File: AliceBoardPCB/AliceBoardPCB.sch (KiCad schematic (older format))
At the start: 1 part

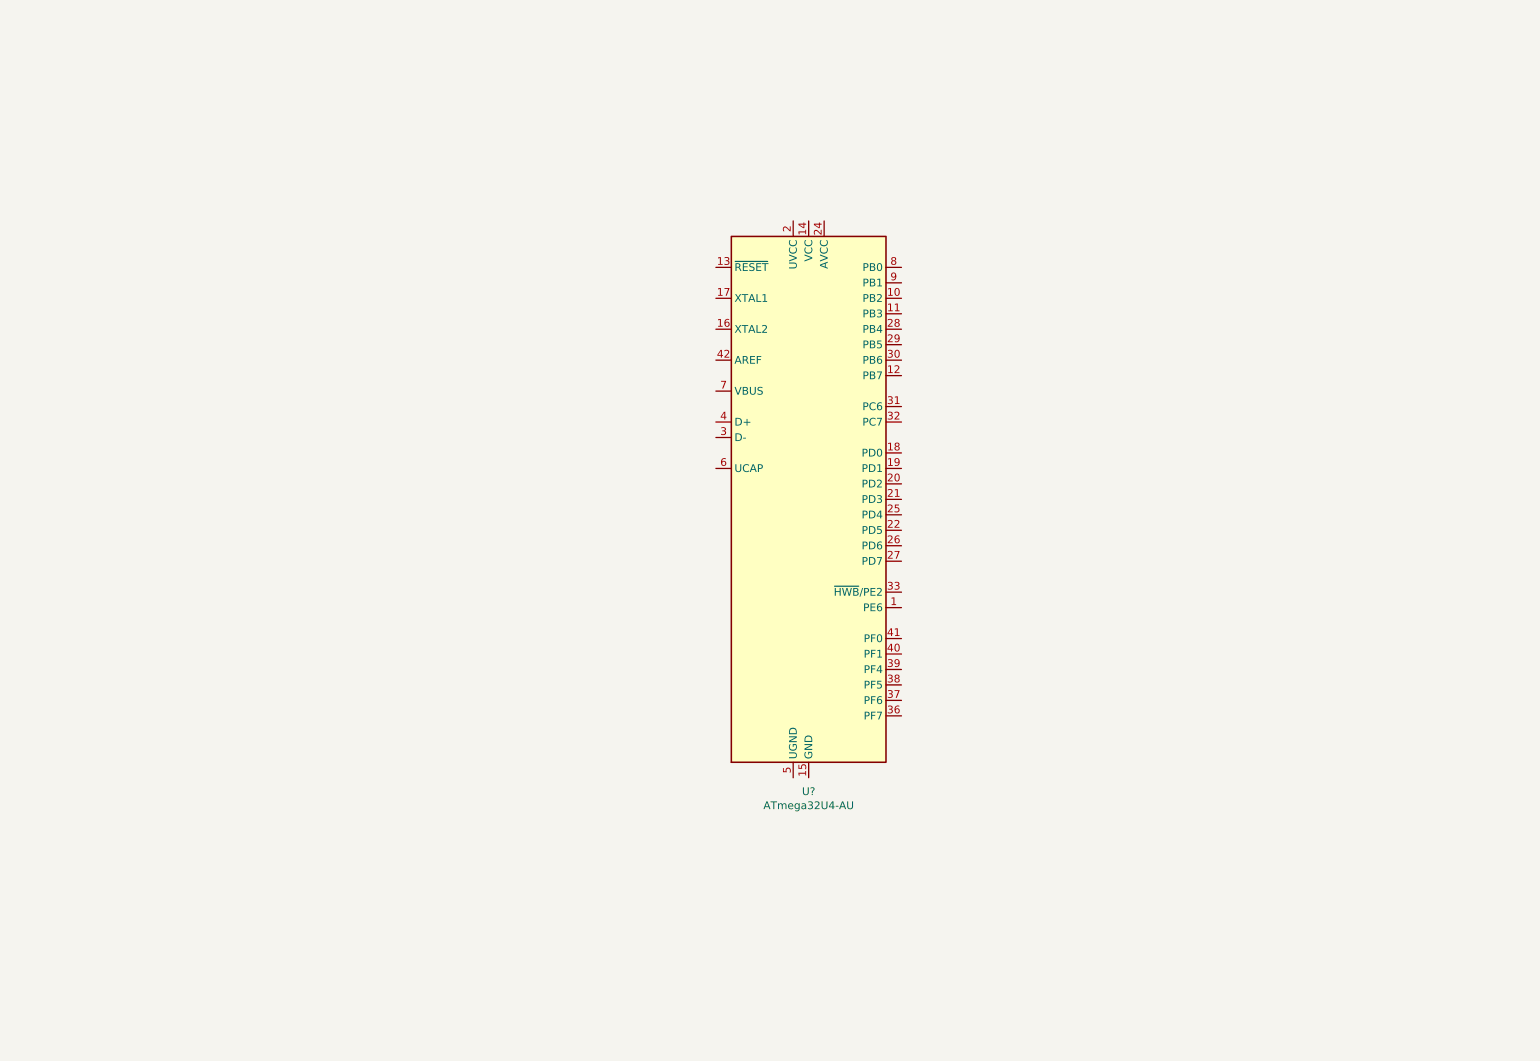
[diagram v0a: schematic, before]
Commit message: Schematic and Acrylic Case
Finished the pcb schematic and im starting the acrylic case.
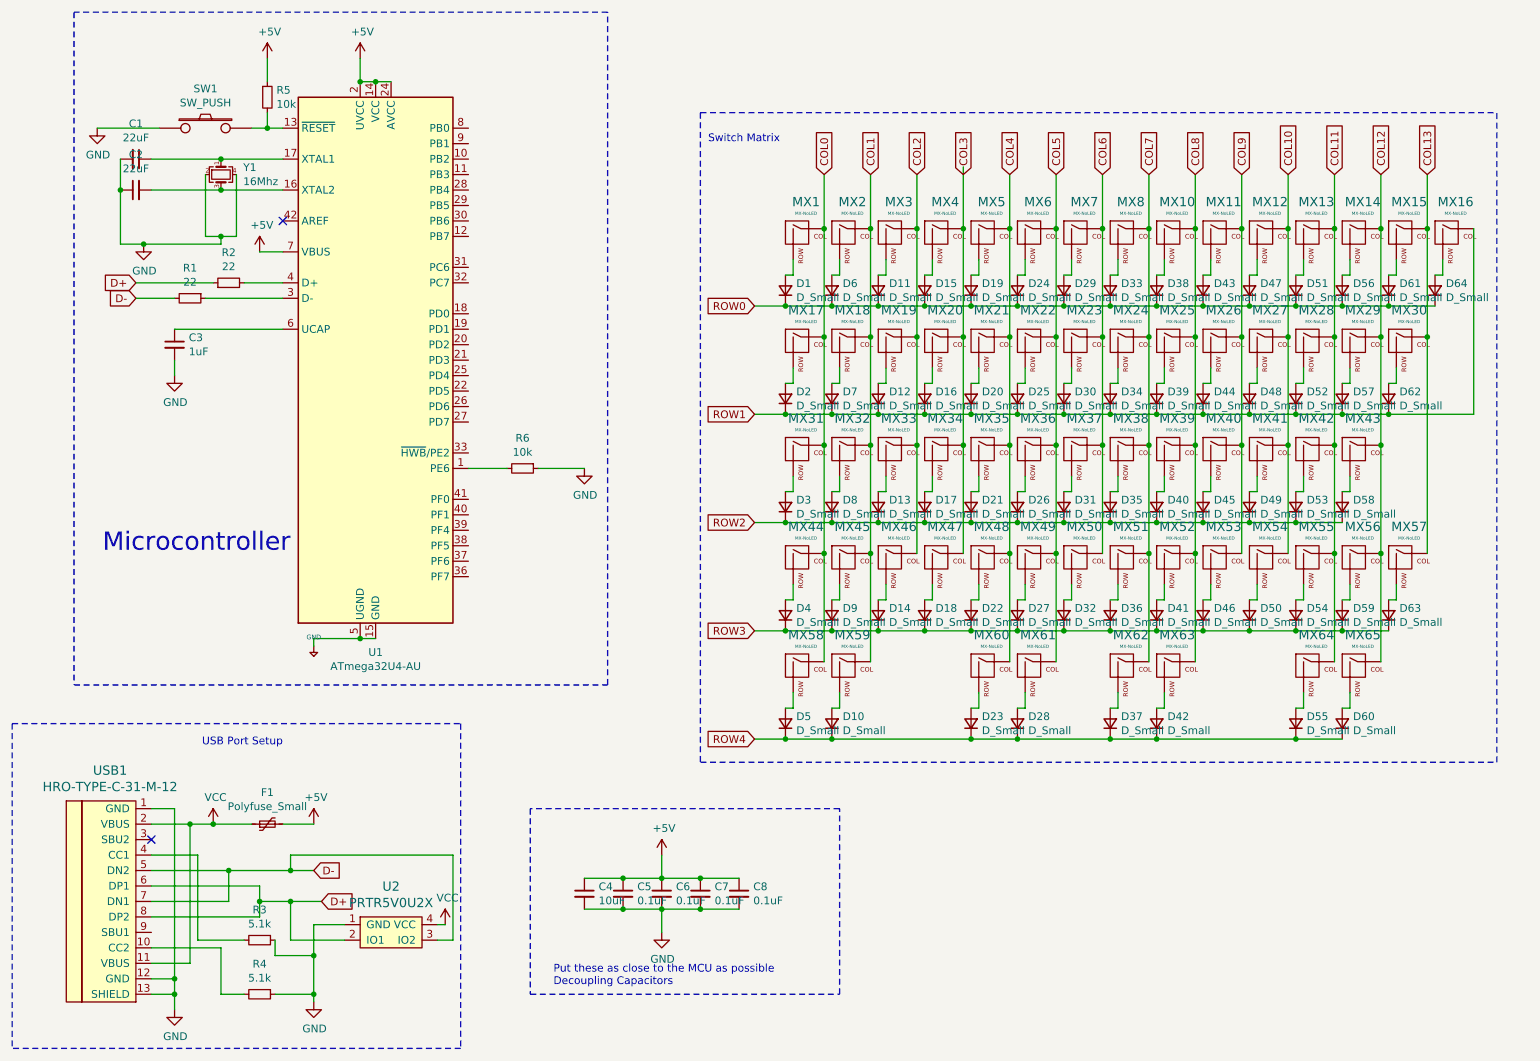
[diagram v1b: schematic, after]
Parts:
- added C1, C2: 22uF, Capacitor_SMD:C_0805_2012Metric, symbol Device:C_Small
- added C3: 1uF, Capacitor_SMD:C_0805_2012Metric, symbol Device:C_Small
- added C4: 10uF, Capacitor_SMD:C_0805_2012Metric, symbol Device:C_Small
- added C5, C6, C7, C8: 0.1uF, Capacitor_SMD:C_0805_2012Metric, symbol Device:C_Small
- added D1, D10, D11, D12, D13, D14, D15, D16, D17, D18, D19, D2, D20, D21, D22, D23, D24, D25, D26, D27, D28, D29, D3, D30, D31, D32, D33, D34, D35, D36, D37, D38, D39, D4, D40, D41, D42, D43, D44, D45, D46, D47, D48, D49, D5, D50, D51, D52, D53, D54, D55, D56, D57, D58, D59, D6, D60, D61, D62, D63, D64, D7, D8, D9: D_Small, Diode_SMD:D_SOD-123, symbol Device:D_Small
- added F1: Polyfuse_Small, Fuse:Fuse_1206_3216Metric, symbol Device:Polyfuse_Small
- added MX1, MX10, MX11, MX12, MX13, MX14, MX15, MX16, MX17, MX18, MX19, MX2, MX20, MX21, MX22, MX23, MX24, MX25, MX26, MX27, MX28, MX29, MX3, MX30, MX31, MX32, MX33, MX34, MX35, MX36, MX37, MX38, MX39, MX4, MX40, MX41, MX42, MX43, MX44, MX45, MX46, MX47, MX48, MX49, MX5, MX50, MX51, MX52, MX53, MX54, MX55, MX56, MX57, MX58, MX59, MX6, MX60, MX61, MX62, MX63, MX64, MX65, MX7, MX8: MX-NoLED, MX_Only:MXOnly-1U-NoLED, symbol MX_Alps_Hybrid:MX-NoLED
- added R1, R2: 22, Resistor_SMD:R_0805_2012Metric, symbol Device:R_Small
- added R3, R4: 5.1k, Resistor_SMD:R_0805_2012Metric, symbol Device:R_Small
- added R5, R6: 10k, Resistor_SMD:R_0805_2012Metric, symbol Device:R_Small
- added SW1: SW_PUSH, random-keyboard-parts:SKQG-1155865, symbol keyboard_parts:SW_PUSH
- added U2: PRTR5V0U2X, random-keyboard-parts:SOT143B, symbol random-keyboard-parts:PRTR5V0U2X
- added USB1: HRO-TYPE-C-31-M-12, Type-C:HRO-TYPE-C-31-M-12, symbol Type-C:HRO-TYPE-C-31-M-12
- added Y1: 16Mhz, Crystal:Crystal_SMD_3225-4Pin_3.2x2.5mm, symbol Device:Crystal_GND24_Small
- gave numbers to parts that had none: 1
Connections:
- net at U1.1 (PE6): now also R6.2
- net at U1.13 (~RESET): now also R5.2, SW1.2
- net +5V: now reaches U1.14 (VCC), U1.34 (VCC)
- net +5V: now also U1.15 (GND), U1.2 (UVCC), U1.23 (GND), U1.24 (AVCC), U1.35 (GND), U1.43 (GND), U1.44 (AVCC), U1.5 (UGND), U1.7 (VBUS), C4.1, C5.1, C6.1, C7.1, C8.1, F1.2, R5.1
- net at U1.16 (XTAL2): now also C2.2, Y1.3
- net at U1.17 (XTAL1): now also C1.1, Y1.1
- net at U1.3 (D-): now also R1.1
- net at U1.4 (D+): now also R2.2
- net at U1.6 (UCAP): now also C3.1
- new net: D1.2 (A), MX1.2 (ROW)
- new net: D6.2 (A), MX2.2 (ROW)
- new net: D11.2 (A), MX3.2 (ROW)
- new net: D15.2 (A), MX4.2 (ROW)
- new net: D19.2 (A), MX5.2 (ROW)
- new net: D24.2 (A), MX6.2 (ROW)
- new net: D29.2 (A), MX7.2 (ROW)
- new net: D33.2 (A), MX8.2 (ROW)
- new net: D38.2 (A), MX10.2 (ROW)
- new net: D43.2 (A), MX11.2 (ROW)
- new net: D47.2 (A), MX12.2 (ROW)
- new net: D51.2 (A), MX13.2 (ROW)
- new net: D56.2 (A), MX14.2 (ROW)
- new net: D61.2 (A), MX15.2 (ROW)
- new net: D64.2 (A), MX16.2 (ROW)
- new net: D2.2 (A), MX17.2 (ROW)
- new net: D7.2 (A), MX18.2 (ROW)
- new net: D12.2 (A), MX19.2 (ROW)
- new net: D16.2 (A), MX20.2 (ROW)
- new net: D20.2 (A), MX21.2 (ROW)
- new net: D25.2 (A), MX22.2 (ROW)
- new net: D30.2 (A), MX23.2 (ROW)
- new net: D34.2 (A), MX24.2 (ROW)
- new net: D39.2 (A), MX25.2 (ROW)
- new net: D44.2 (A), MX26.2 (ROW)
- new net: D48.2 (A), MX27.2 (ROW)
- new net: D52.2 (A), MX28.2 (ROW)
- new net: D57.2 (A), MX29.2 (ROW)
- new net: D62.2 (A), MX30.2 (ROW)
- new net: D3.2 (A), MX31.2 (ROW)
- new net: D8.2 (A), MX32.2 (ROW)
- new net: D13.2 (A), MX33.2 (ROW)
- new net: D17.2 (A), MX34.2 (ROW)
- new net: D21.2 (A), MX35.2 (ROW)
- new net: D26.2 (A), MX36.2 (ROW)
- new net: D31.2 (A), MX37.2 (ROW)
- new net: D35.2 (A), MX38.2 (ROW)
- new net: D40.2 (A), MX39.2 (ROW)
- new net: D45.2 (A), MX40.2 (ROW)
- new net: D49.2 (A), MX41.2 (ROW)
- new net: D53.2 (A), MX42.2 (ROW)
- new net: D58.2 (A), MX43.2 (ROW)
- new net: D4.2 (A), MX44.2 (ROW)
- new net: D9.2 (A), MX45.2 (ROW)
- new net: D14.2 (A), MX46.2 (ROW)
- new net: D18.2 (A), MX47.2 (ROW)
- new net: D22.2 (A), MX48.2 (ROW)
- new net: D27.2 (A), MX49.2 (ROW)
- new net: D32.2 (A), MX50.2 (ROW)
- new net: D36.2 (A), MX51.2 (ROW)
- new net: D41.2 (A), MX52.2 (ROW)
- new net: D46.2 (A), MX53.2 (ROW)
- new net: D50.2 (A), MX54.2 (ROW)
- new net: D54.2 (A), MX55.2 (ROW)
- new net: D59.2 (A), MX56.2 (ROW)
- new net: D5.2 (A), MX58.2 (ROW)
- new net: D10.2 (A), MX59.2 (ROW)
- new net: D23.2 (A), MX60.2 (ROW)
- new net: D28.2 (A), MX61.2 (ROW)
- new net: D37.2 (A), MX62.2 (ROW)
- new net: D42.2 (A), MX63.2 (ROW)
- new net: D55.2 (A), MX64.2 (ROW)
- new net: D60.2 (A), MX65.2 (ROW)
- new net: D63.2 (A), MX57.2 (ROW)
- new net: R4.2, USB1.10 (CC2)
- new net: R3.2, USB1.4 (CC1)
- new net COL0: MX1.1 (COL), MX17.1 (COL), MX31.1 (COL), MX44.1 (COL), MX58.1 (COL)
- new net COL1: MX18.1 (COL), MX2.1 (COL), MX32.1 (COL), MX45.1 (COL), MX59.1 (COL)
- new net COL10: MX12.1 (COL), MX27.1 (COL), MX41.1 (COL), MX54.1 (COL)
- new net COL11: MX13.1 (COL), MX28.1 (COL), MX42.1 (COL), MX55.1 (COL), MX64.1 (COL)
- new net COL12: MX14.1 (COL), MX29.1 (COL), MX43.1 (COL), MX56.1 (COL), MX65.1 (COL)
- new net COL13: MX15.1 (COL), MX30.1 (COL), MX57.1 (COL)
- new net COL2: MX19.1 (COL), MX3.1 (COL), MX33.1 (COL), MX46.1 (COL)
- new net COL3: MX20.1 (COL), MX34.1 (COL), MX4.1 (COL), MX47.1 (COL)
- new net COL4: MX21.1 (COL), MX35.1 (COL), MX48.1 (COL), MX5.1 (COL), MX60.1 (COL)
- new net COL5: MX22.1 (COL), MX36.1 (COL), MX49.1 (COL), MX6.1 (COL), MX61.1 (COL)
- new net COL6: MX23.1 (COL), MX37.1 (COL), MX50.1 (COL), MX7.1 (COL)
- new net COL7: MX24.1 (COL), MX38.1 (COL), MX51.1 (COL), MX62.1 (COL), MX8.1 (COL)
- new net COL8: MX10.1 (COL), MX25.1 (COL), MX39.1 (COL), MX52.1 (COL), MX63.1 (COL)
- new net COL9: MX11.1 (COL), MX26.1 (COL), MX40.1 (COL), MX53.1 (COL)
- new net D+: R2.1, U2.2 (IO1), USB1.6 (DP1), USB1.8 (DP2)
- new net D-: R1.2, U2.3 (IO2), USB1.5 (DN2), USB1.7 (DN1)
- new net GND: C1.2, C2.1, C3.2, C4.2, C5.2, C6.2, C7.2, C8.2, R3.1, R4.1, R6.1, SW1.1, U2.1 (GND), USB1.1 (GND), USB1.12 (GND), USB1.13 (SHIELD), Y1.2, Y1.4
- new net ROW0: D1.1 (K), D11.1 (K), D15.1 (K), D19.1 (K), D24.1 (K), D29.1 (K), D33.1 (K), D38.1 (K), D43.1 (K), D47.1 (K), D51.1 (K), D56.1 (K), D6.1 (K), D61.1 (K), D64.1 (K)
- new net ROW1: D12.1 (K), D16.1 (K), D2.1 (K), D20.1 (K), D25.1 (K), D30.1 (K), D34.1 (K), D39.1 (K), D44.1 (K), D48.1 (K), D52.1 (K), D57.1 (K), D62.1 (K), D7.1 (K), MX16.1 (COL)
- new net ROW2: D13.1 (K), D17.1 (K), D21.1 (K), D26.1 (K), D3.1 (K), D31.1 (K), D35.1 (K), D40.1 (K), D45.1 (K), D49.1 (K), D53.1 (K), D58.1 (K), D8.1 (K)
- new net ROW3: D14.1 (K), D18.1 (K), D22.1 (K), D27.1 (K), D32.1 (K), D36.1 (K), D4.1 (K), D41.1 (K), D46.1 (K), D50.1 (K), D54.1 (K), D59.1 (K), D63.1 (K), D9.1 (K)
- new net ROW4: D10.1 (K), D23.1 (K), D28.1 (K), D37.1 (K), D42.1 (K), D5.1 (K), D55.1 (K), D60.1 (K)
- new net VCC: F1.1, U2.4 (VCC), USB1.11 (VBUS), USB1.2 (VBUS)
- no-connect marks 0 -> 2
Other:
- note added: "Microcontroller"
- note added: "Put these as close to the MCU as possible\nDecoupling Capacitors"
- note added: "Switch Matrix"
- note added: "USB Port Setup"
- moved on the sheet: U1

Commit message: Switch Matrix PCB Layour
Finished up the PCB layout for the switch matrix. I just have to do the wire routing and placement of the processing components.  Its going well!
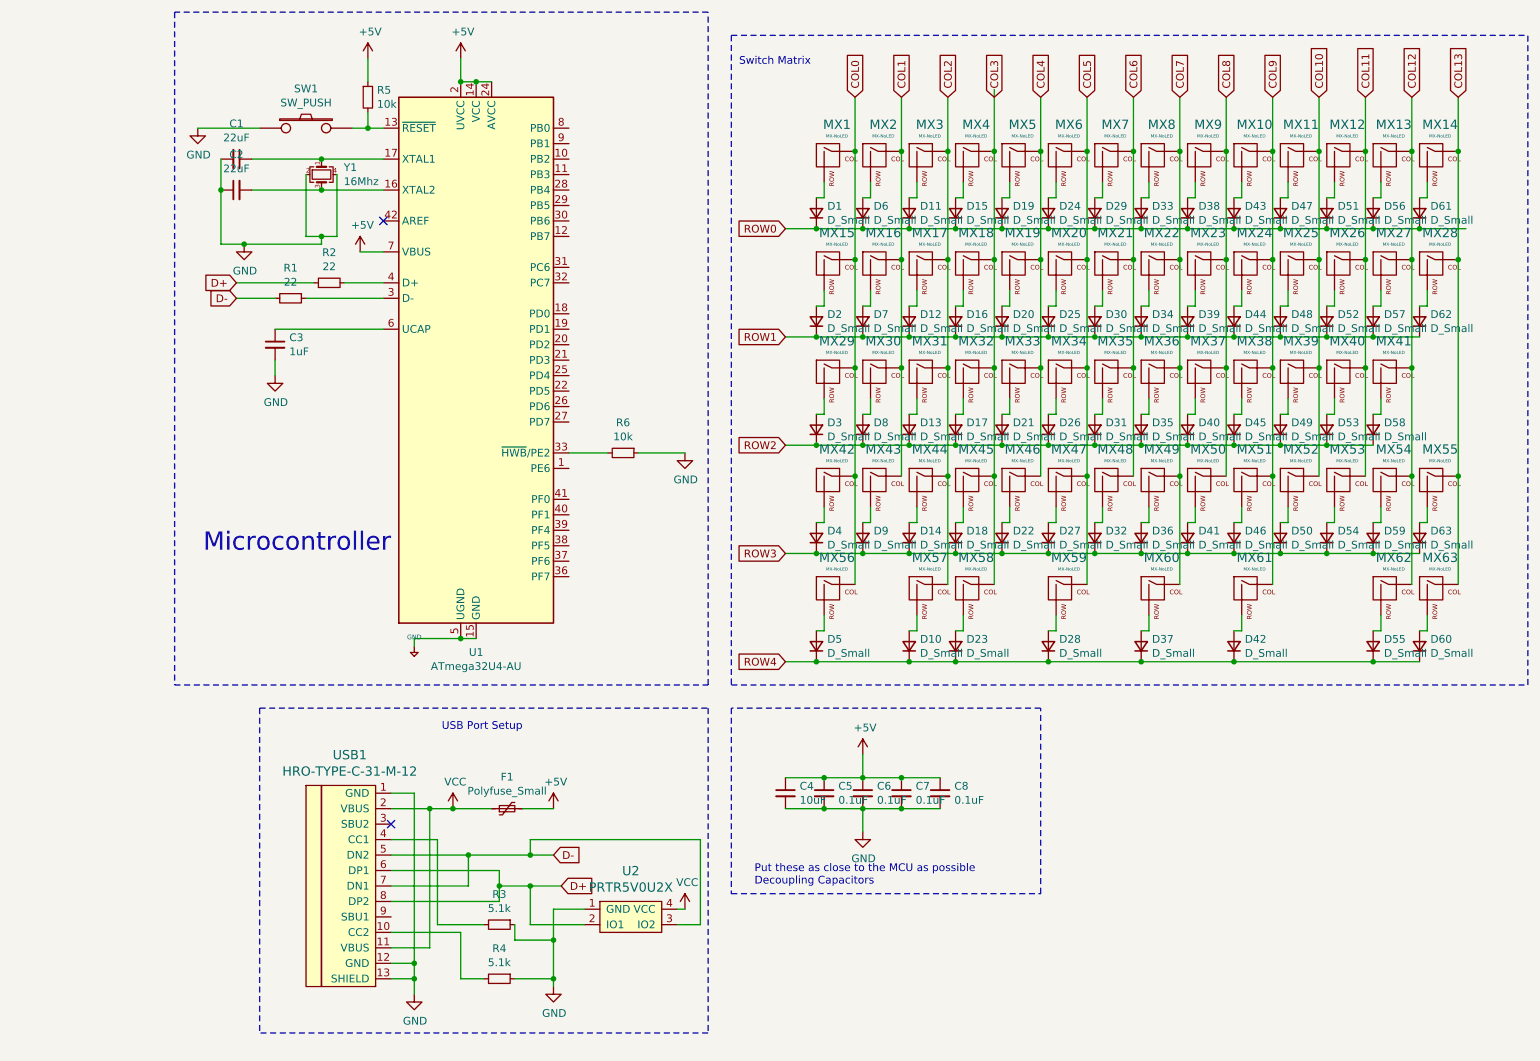
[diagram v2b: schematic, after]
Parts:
- removed D64: D_Small, Diode_SMD:D_SOD-123, symbol Device:D_Small
- removed MX16: MX-NoLED, MX_Only:MXOnly-1U-NoLED, symbol MX_Alps_Hybrid:MX-NoLED
- renumbered MX11 to MX10, MX12 to MX11, MX13 to MX12, MX14 to MX13, MX15 to MX14, MX17 to MX15, MX18 to MX16, MX19 to MX17, MX20 to MX18, MX21 to MX19, MX22 to MX20, MX23 to MX21, MX24 to MX22, MX25 to MX23, MX26 to MX24, MX27 to MX25, MX28 to MX26, MX29 to MX27, MX30 to MX28, MX31 to MX29, MX32 to MX30, MX33 to MX31, MX34 to MX32, MX35 to MX33, MX36 to MX34, MX37 to MX35, MX38 to MX36, MX39 to MX37, MX40 to MX38, MX41 to MX39, MX42 to MX40, MX43 to MX41, MX44 to MX42, MX45 to MX43, MX46 to MX44, MX47 to MX45, MX48 to MX46, MX49 to MX47, MX50 to MX48, MX51 to MX49, MX52 to MX50, MX53 to MX51, MX54 to MX52, MX55 to MX53, MX56 to MX54, MX57 to MX55, MX58 to MX56, MX59 to MX57, MX60 to MX58, MX61 to MX59, MX62 to MX60, MX63 to MX61, MX64 to MX62, MX65 to MX63, MX10 to MX9
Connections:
- net COL1: no longer MX57.1 (COL)
- net COL11: no longer MX62.1 (COL)
- net COL12: now also MX62.1 (COL); no longer MX63.1 (COL)
- net COL13: now also MX63.1 (COL)
- net COL2: now also MX57.1 (COL)
- net COL3: now also MX58.1 (COL)
- net COL4: no longer MX58.1 (COL)
- net COL8: no longer MX61.1 (COL)
- net COL9: now also MX61.1 (COL)
- net at U1.1 (PE6): no longer R6.2
- net at U1.33 (~HWB~/PE2): now also R6.2
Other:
- moved on the sheet: C1, C2, C3, C4, C5, C6, C7, C8, D1, D10, D11, D12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
